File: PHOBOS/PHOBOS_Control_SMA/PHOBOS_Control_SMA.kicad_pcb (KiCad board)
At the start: 4 copper layers, 58.4 x 35.6 mm, 82 parts, among them IC10 PD2328J5050S2HF, IC4 MAPS-010144-TR0500, IC5 MAPS-010144-TR0500, IC6 MAPS-010144-TR0500, IC7 MAPS-010144-TR0500, IC8 PD2328J5050S2HF, IC9 PD2328J5050S2HF, J1 ANT3, J2 ANT4, J3 USB4056-03-A_REVA2, J4 BATT, J5 ANT1, J6 ANT2, J8 BOOT, U1 SX1280IMLTRT, U2 W25Q128JVSIQ, U3 NCP1117-3.3_SOT223, U4 RP2040, U5 TPS60403DBV, Y1 C1E-52.000-10-1012-X-M, Y2 ABM8-272-T3

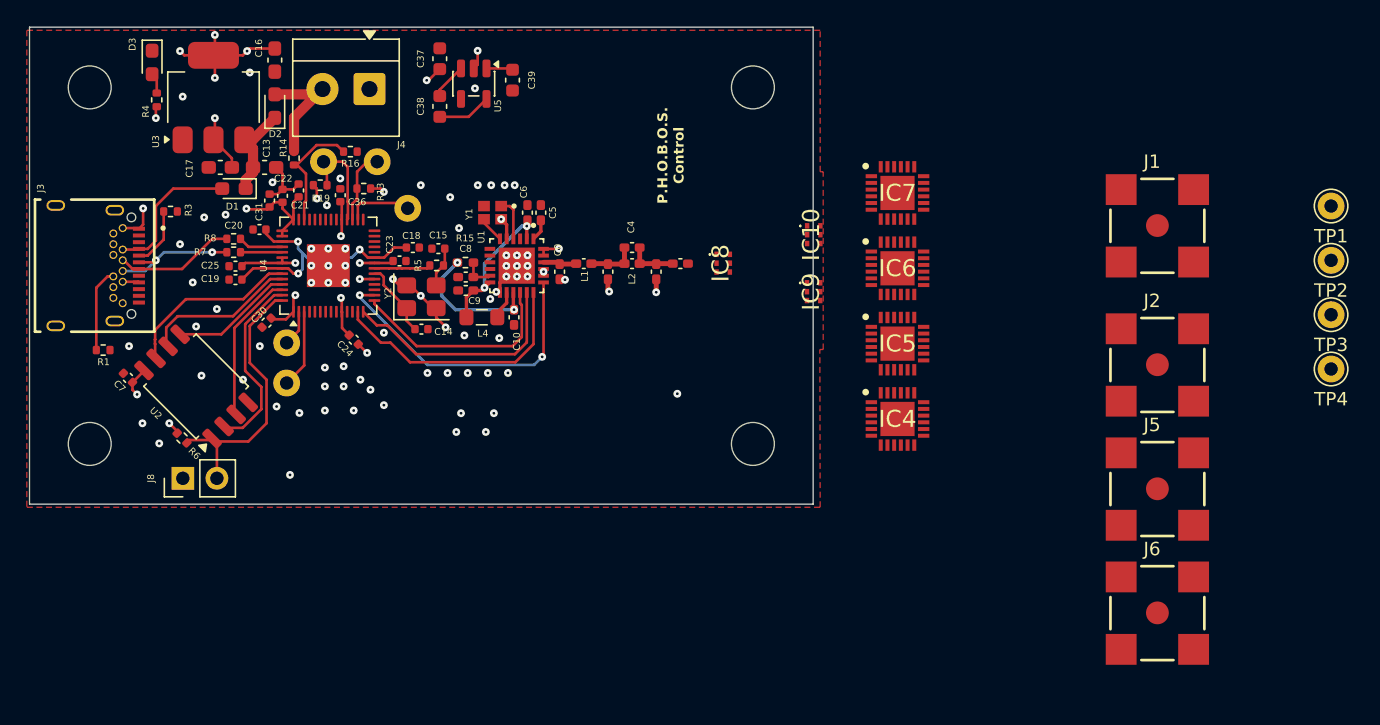
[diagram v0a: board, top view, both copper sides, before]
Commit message: sensors added to schematic and board. unlayed
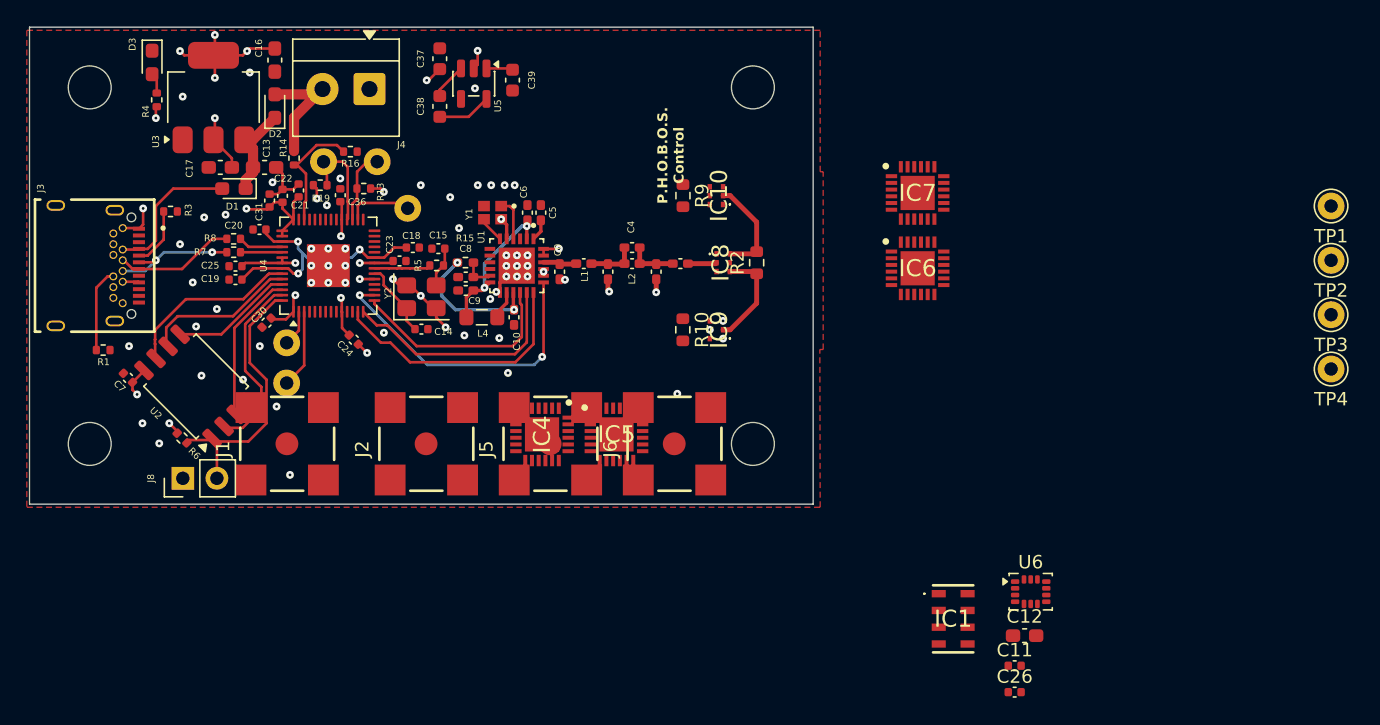
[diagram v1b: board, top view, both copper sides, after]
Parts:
- added C11: 100n, Capacitor_SMD:C_0402_1005Metric, F.Cu at (203.8, 128.2)
- added C12: 10u, Capacitor_SMD:C_0603_1608Metric_Pad1.08x0.95mm_HandSolder, F.Cu at (204.6, 126.0)
- added C26: 100n, Capacitor_SMD:C_0402_1005Metric, F.Cu at (203.8, 130.2)
- added IC1: MPL3115A2ST1, MPL3115A2ST1:MPL3115A2ST1, F.Cu at (199.2, 124.7)
- added R10: 100, Resistor_SMD:R_0603_1608Metric, F.Cu at (179.1, 103.2)
- added R2: 100, Resistor_SMD:R_0603_1608Metric, F.Cu at (184.6, 98.2)
- added R9: 100, Resistor_SMD:R_0603_1608Metric, F.Cu at (179.1, 93.2)
- added U6: LSM6DS3, Package_LGA:LGA-14_3x2.5mm_P0.5mm_LayoutBorder3x4y, F.Cu at (205.0, 122.7)
- moved J1 66.9 mm to (149.6, 111.7), turned to 90 degrees
- moved J2 54.8 mm to (160.0, 111.7), turned to 90 degrees
- moved J5 45.4 mm to (169.2, 111.7), turned to 90 degrees
- moved J6 38.1 mm to (178.5, 111.7), turned to 90 degrees
- moved IC4 26.5 mm to (168.6, 111.0), turned to -90 degrees
- moved IC5 22.0 mm to (174.1, 111.0)
- moved IC10 7.82 mm to (181.6, 93.2), turned to -90 degrees
- moved IC9 7.78 mm to (181.6, 103.2), turned to -90 degrees
- moved IC6 1.50 mm to (196.6, 98.6)
- moved IC7 1.50 mm to (196.6, 93.0)
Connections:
- IC10 pad 3: GND -> Net-(IC10-GND_2)
- IC10 pad 5: GND -> Net-(IC10-GND_2)
- IC8 pad 3: GND -> Net-(IC8-GND_2)
- IC8 pad 5: GND -> Net-(IC8-GND_2)
- IC9 pad 3: GND -> Net-(IC9-GND_2)
- IC9 pad 5: GND -> Net-(IC9-GND_2)
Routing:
- net /RFO2: track 0.00 -> 7.59 mm
- net /RFO1: track 0.00 -> 7.59 mm
- net /RFO: track 0.00 -> 2.16 mm
- net GND: vias 82 -> 67
